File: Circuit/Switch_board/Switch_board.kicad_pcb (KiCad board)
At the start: 2 copper layers, 40 x 31.7 mm, 31 parts, among them J1 switch_mode, J2 switch, M3 MountingHole_3mm, P1 XT30, Q1 2N7002, Q2 2N7002, Q3 2N7002, Q4 2N7002, U1 DRV5023

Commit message: Switch_board Rev1.1 was routed
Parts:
- added D6: BZT52C12S, Diodes_SMD:D_SOD-323_HandSoldering, F.Cu at (149.9, 111.5)
- added Q5: RSC002P03, TO_SOT_Packages_SMD:SOT-23_Handsoldering, F.Cu at (147.1, 115.1)
- added R13: 10k, Resistors_SMD:R_0603_HandSoldering, F.Cu at (154.8, 111.5)
- added R14: 100, Resistors_SMD:R_0603_HandSoldering, B.Cu at (159.7, 119.9)
- D1: value BZX585-C12 -> BZT52C12S; footprint Diodes_SMD:D_SOD-523 -> Diodes_SMD:D_SOD-323_HandSoldering
- J2: value switch -> switch_connector
- P1: value XT30 -> power_in
- moved R1 5.18 mm to (164.4, 117.6)
- moved D1 0.70 mm to (169.9, 112.1)
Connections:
- C1 pad 1: VCC -> Net-(C1-Pad1)
- P1 pad 1: VCC -> Net-(P1-Pad1)
- U1 pad 1: VCC -> Net-(C1-Pad1)
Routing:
- net Net-(D6-Pad2): track 0.00 -> 8.44 mm
- net Net-(P1-Pad1): track 0.00 -> 6.78 mm
- net Net-(C1-Pad1): track 0.00 -> 6.71 mm
- net VCC: track 44.5 -> 45.4 mm
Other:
- board text added: "ZEABUS 2018 Switch_board Rev1.1"
- board text removed: "ZEABUS 2018 Switch_board"

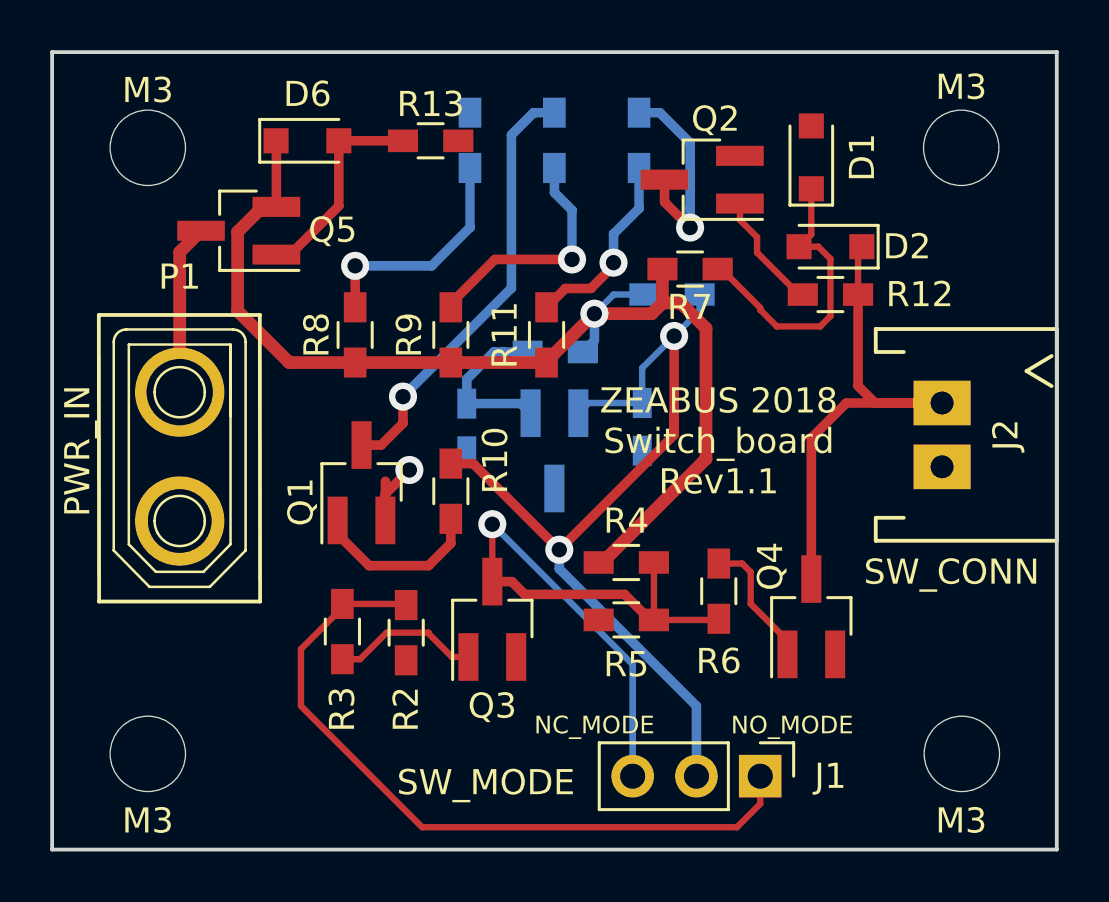
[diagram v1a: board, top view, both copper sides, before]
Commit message: exchanged 90136-1202 footprint on Switch_board pcb
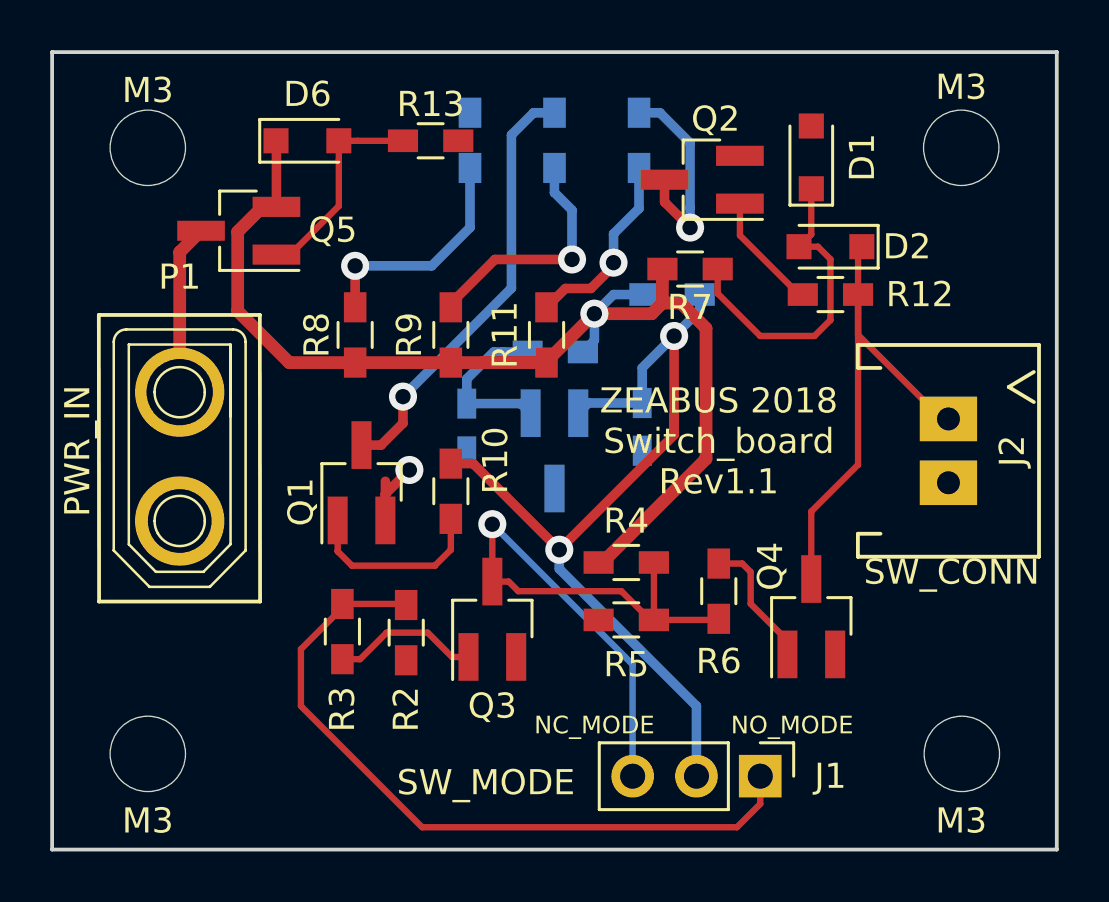
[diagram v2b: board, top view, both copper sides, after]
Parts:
- moved J2 0.68 mm to (175.4, 123.8)
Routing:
- net Net-(D1-Pad1): track 11.9 -> 13.0 mm
- net +switch: track 21.5 -> 20.7 mm
- net Net-(J1-Pad3): track 27.6 -> 26.9 mm
- net Net-(Q1-Pad1): track 6.92 -> 7.47 mm
